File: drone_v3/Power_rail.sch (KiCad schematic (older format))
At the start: 9 parts, among them J10 Conn_01x08_Male, J11 Conn_01x04_Male, J12 Conn_01x08_Male, J13 Conn_01x08_Male, J14 Conn_01x02_Male, J16 Conn_01x03_Male, J17 Conn_01x02_Male, Q2 2N3904

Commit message: add alot
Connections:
- net +5V: now also J13.1 (Pin_1), J13.2 (Pin_2), J13.3 (Pin_3), J13.4 (Pin_4), J13.5 (Pin_5), J13.6 (Pin_6), J13.7 (Pin_7), J13.8 (Pin_8)
- net VCC: no longer J13.1 (Pin_1), J13.2 (Pin_2), J13.3 (Pin_3), J13.4 (Pin_4), J13.5 (Pin_5), J13.6 (Pin_6), J13.7 (Pin_7), J13.8 (Pin_8)
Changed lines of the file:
@@
 Wire Wire Line
 	4500 4200 4500 4100
-Connection ~ 4500 3500
 Wire Wire Line
 	4500 3500 4500 3350
@@
 Wire Wire Line
 	4500 4100 4500 4000
-$Comp
-L power:VCC #PWR?
-U 1 1 5F4381B7
-P 4500 3350
-AR Path="/5F4381B7" Ref="#PWR?"  Part="1"
-AR Path="/5F41B667/5F4381B7" Ref="#PWR0132"  Part="1"
-F 0 "#PWR0132" H 4500 3200 50  0001 C CNN
-F 1 "VCC" H 4515 3523 50  0000 C CNN
-F 2 "" H 4500 3350 50  0001 C CNN
-F 3 "" H 4500 3350 50  0001 C CNN
-	1    4500 3350
-	1    0    0    -1
-$EndComp
 Text GLabel 3800 4000 0    50   Input ~ 0
 TIM3_CH3
@@
 Text GLabel 3800 3500 0    50   Input ~ 0
 USB_D+
+Connection ~ 4500 3500
+$Comp
+L power:+5V #PWR?
+U 1 1 5F35A86E
+P 4500 3350
+AR Path="/5F35A86E" Ref="#PWR?"  Part="1"
+AR Path="/5F41B667/5F35A86E" Ref="#PWR0174"  Part="1"
+F 0 "#PWR0174" H 4500 3200 50  0001 C CNN
+F 1 "+5V" H 4515 3523 50  0000 C CNN
+F 2 "" H 4500 3350 50  0001 C CNN
+F 3 "" H 4500 3350 50  0001 C CNN
+	1    4500 3350
+	1    0    0    -1
+$EndComp
 $EndSCHEMATC

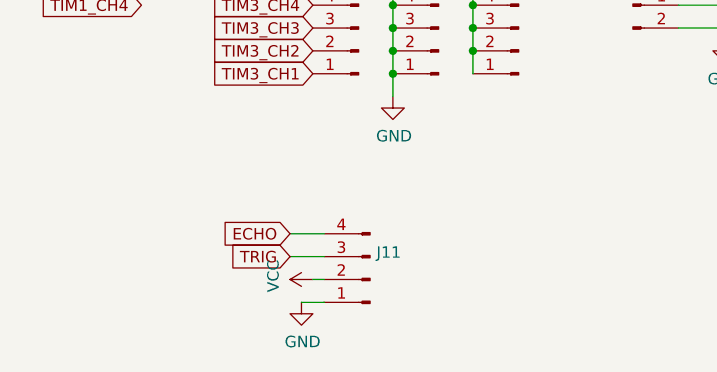
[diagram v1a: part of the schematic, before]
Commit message: cystal layout
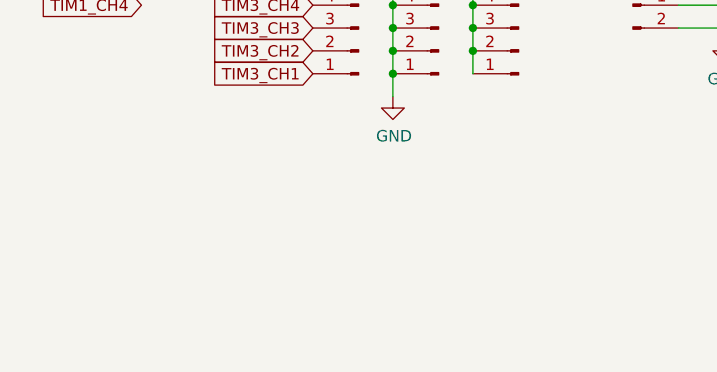
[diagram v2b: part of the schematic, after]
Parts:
- removed J11: Conn_01x04_Male, Connector_PinHeader_2.54mm:PinHeader_1x04_P2.54mm_Vertical, symbol Connector:Conn_01x04_Male
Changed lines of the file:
@@
 	1    0    0    -1
-$EndComp
-Wire Wire Line
-	3850 5200 3750 5200
-$Comp
-L power:GND #PWR?
-U 1 1 5F54FB15
-P 3750 5200
-AR Path="/5F54FB15" Ref="#PWR?"  Part="1"
-AR Path="/5F41B667/5F54FB15" Ref="#PWR0137"  Part="1"
-F 0 "#PWR0137" H 3750 4950 50  0001 C CNN
-F 1 "GND" H 3755 5027 50  0000 C CNN
-F 2 "" H 3750 5200 50  0001 C CNN
-F 3 "" H 3750 5200 50  0001 C CNN
-	1    3750 5200
-	1    0    0    -1
-$EndComp
-Wire Wire Line
-	3850 5100 3800 5100
-$Comp
-L power:VCC #PWR?
-U 1 1 5F54FB1C
-P 3800 5100
-AR Path="/5F54FB1C" Ref="#PWR?"  Part="1"
-AR Path="/5F41B667/5F54FB1C" Ref="#PWR0138"  Part="1"
-F 0 "#PWR0138" H 3800 4950 50  0001 C CNN
-F 1 "VCC" H 3815 5273 50  0000 C CNN
-F 2 "" H 3800 5100 50  0001 C CNN
-F 3 "" H 3800 5100 50  0001 C CNN
-	1    3800 5100
-	0    -1   -1   0
-$EndComp
-Wire Wire Line
-	3700 5000 3850 5000
-Wire Wire Line
-	3700 4900 3850 4900
-Text GLabel 3700 5000 0    50   Input ~ 0
-TRIG
-Text GLabel 3700 4900 0    50   Input ~ 0
-ECHO
-$Comp
-L Connector:Conn_01x04_Male J?
-U 1 1 5F54FB26
-P 4050 5100
-AR Path="/5F54FB26" Ref="J?"  Part="1"
-AR Path="/5F41B667/5F54FB26" Ref="J11"  Part="1"
-F 0 "J11" H 4022 4982 50  0000 R CNN
-F 1 "Conn_01x04_Male" H 4022 5073 50  0001 R CNN
-F 2 "Connector_PinHeader_2.54mm:PinHeader_1x04_P2.54mm_Vertical" H 4050 5100 50  0001 C CNN
-F 3 "~" H 4050 5100 50  0001 C CNN
-	1    4050 5100
-	-1   0    0    1
 $EndComp
 Text GLabel 7950 3900 0    50   Input ~ 0

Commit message: add alot
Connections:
- net USB_D+: no longer names the net of J10.8 (Pin_8)
- no-connect marks 0 -> 1
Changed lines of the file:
@@
 Wire Wire Line
 	8650 3250 8650 3500
-Text GLabel 3800 3500 0    50   Input ~ 0
-USB_D+
 Connection ~ 4500 3500
 $Comp
@@
 	1    0    0    -1
 $EndComp
+NoConn ~ 3800 3500
 $EndSCHEMATC
